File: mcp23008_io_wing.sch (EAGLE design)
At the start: 16 parts

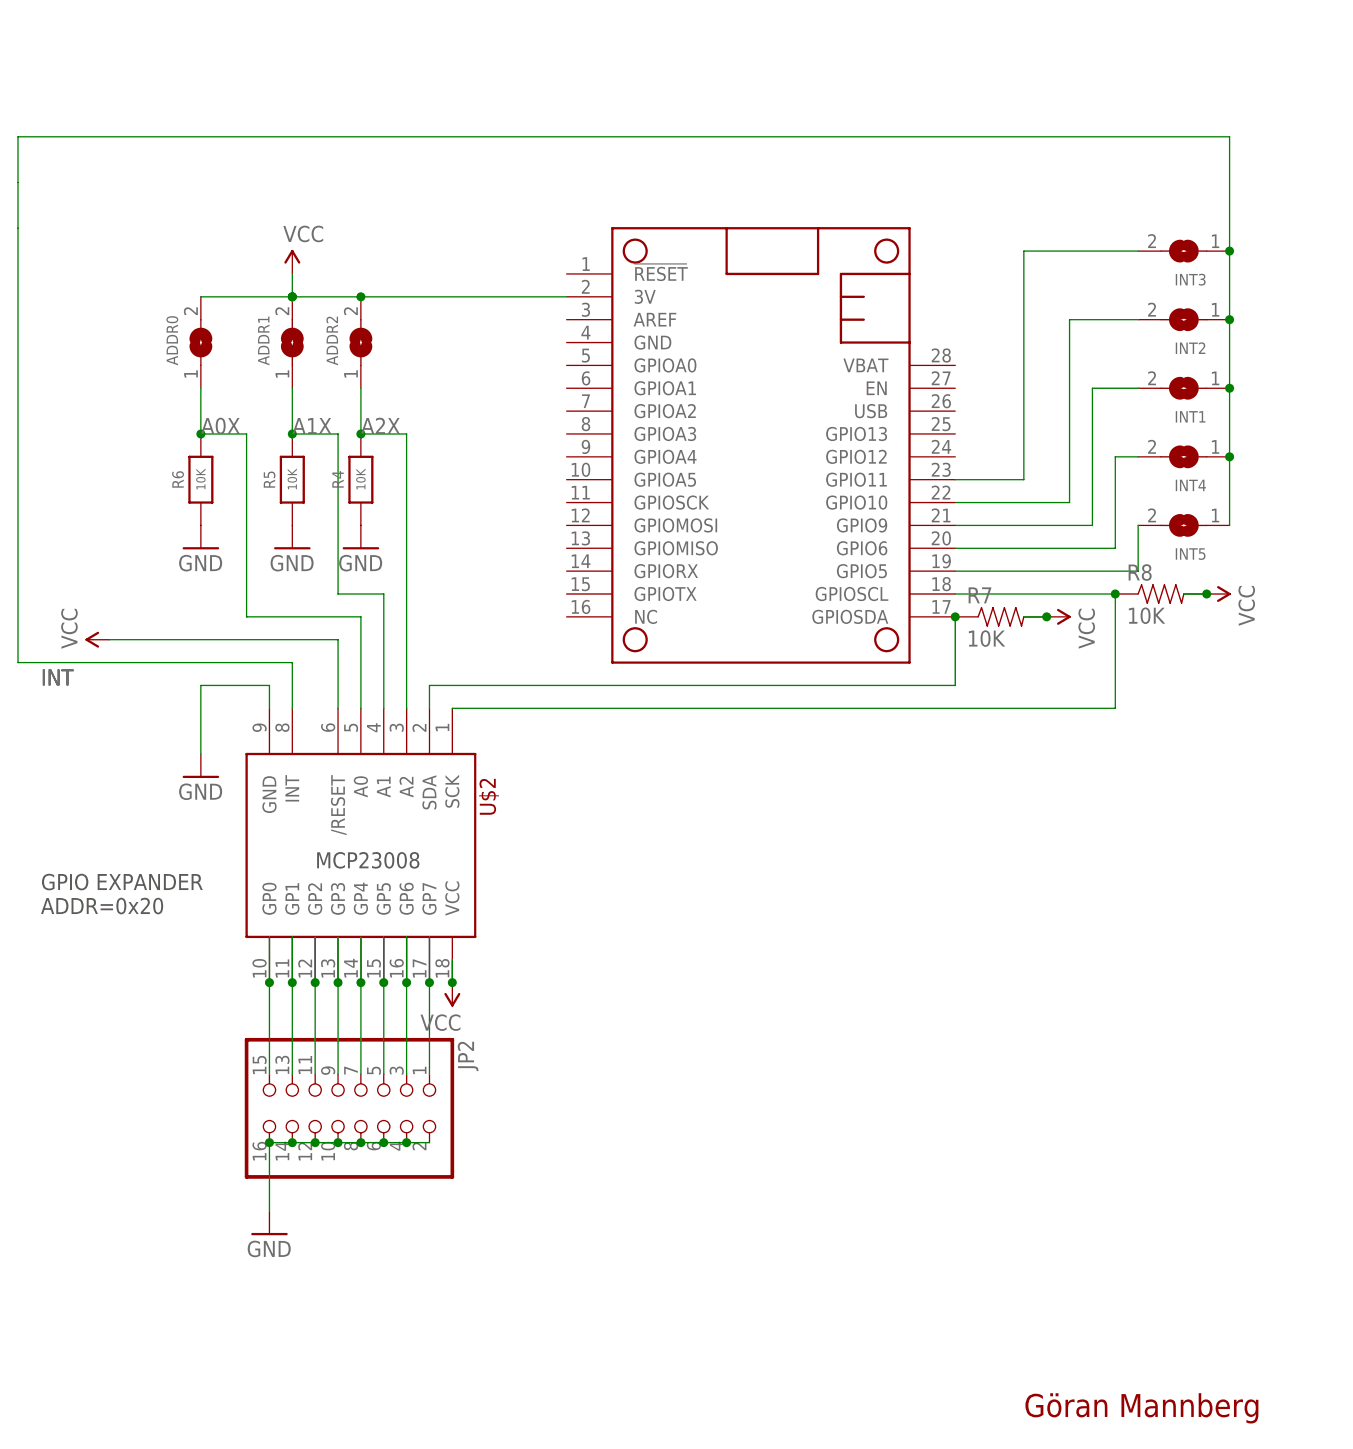
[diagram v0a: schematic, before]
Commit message: updated board and pcb images
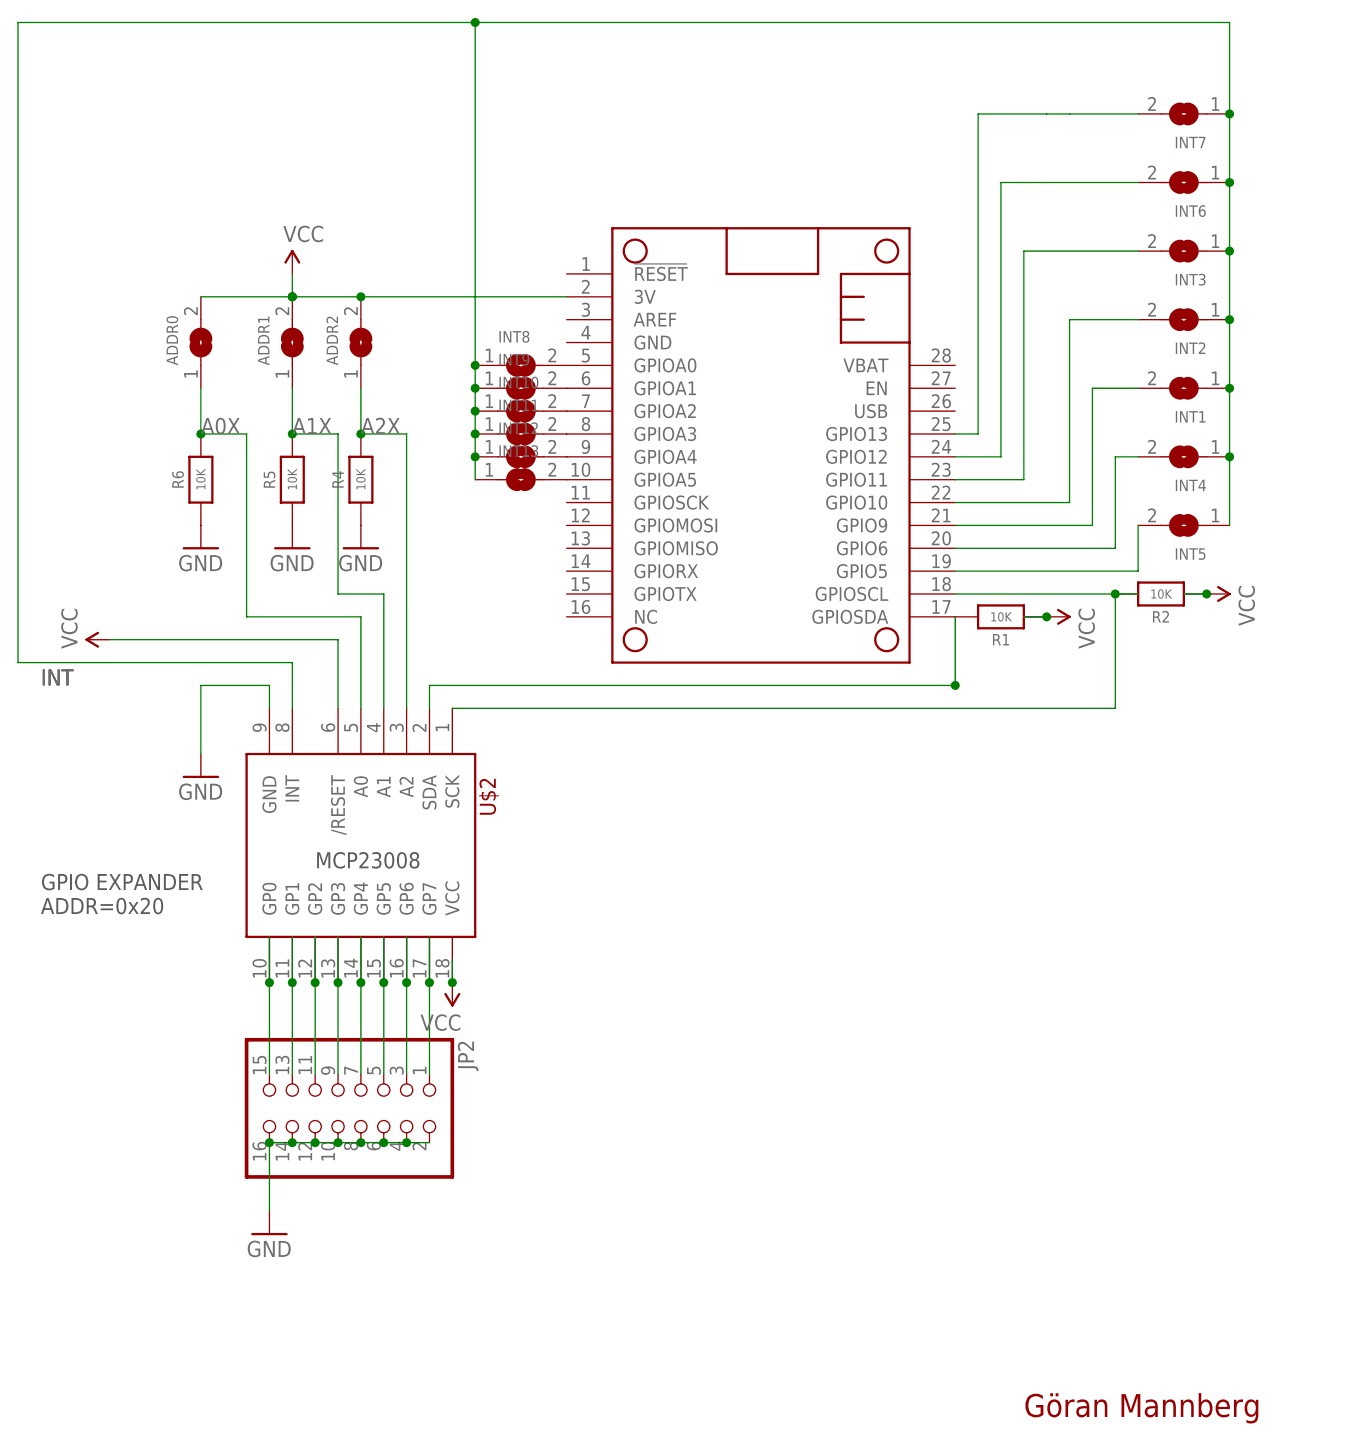
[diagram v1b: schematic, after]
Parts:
- removed R7, R8: 10K, rickk2:RES-10K-06030603
- added INT10, INT11, INT12, INT13, INT6, INT7, INT8, INT9: (no value), microbuilder:SOLDERJUMPER
- added R1, R2: 10K, microbuilder:RESISTOR_0603_NOOUT
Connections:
- new net N$10: INT10.2, MS1.GPIOA2
- new net N$11: INT11.2, MS1.GPIOA3
- new net N$12: INT12.2, MS1.GPIOA4
- new net N$13: INT13.2, MS1.GPIOA5
- new net N$4: INT6.2, MS1.GPIO12
- new net N$5: INT7.2, MS1.GPIO13
- new net N$6: INT8.2, MS1.GPIOA0
- new net N$9: INT9.2, MS1.GPIOA1
- net 3V: now also R1.1, R2.1; no longer R7.2, R8.2
- net INT: now also INT10.1, INT11.1, INT12.1, INT13.1, INT6.1, INT7.1, INT8.1, INT9.1
- net SCL: now also R2.2; no longer R8.1
- net SDA: now also R1.2; no longer R7.1

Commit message: pcb v2
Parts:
- removed R1, R2: 10K, microbuilder:RESISTOR_0603_NOOUT
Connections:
- removed net VCC: U$2./RESET
- net 3V: now also U$2./RESET; no longer R1.1, R2.1
- net SCL: no longer R2.2
- net SDA: no longer R1.2
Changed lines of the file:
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@@
 <part name="SUPPLY1" library="rickk2" deviceset="VCC" device=""/>
 <part name="GND3" library="rickk2" deviceset="GND" device=""/>
-<part name="SUPPLY2" library="rickk2" deviceset="VCC" device=""/>
-<part name="SUPPLY3" library="rickk2" deviceset="VCC" device=""/>
 <part name="SUPPLY4" library="rickk2" deviceset="VCC" device=""/>
-<part name="SUPPLY5" library="rickk2" deviceset="VCC" device=""/>
 <part name="JP2" library="microbuilder" deviceset="HEADER-2X8" device="_SHROUDED"/>
 <part name="GND2" library="rickk2" deviceset="GND" device=""/>
@@
 <part name="INT12" library="microbuilder" deviceset="SOLDERJUMPER" device=""/>
 <part name="INT13" library="microbuilder" deviceset="SOLDERJUMPER" device=""/>
-<part name="R1" library="microbuilder" deviceset="RESISTOR" device="_0603_NOOUT" value="10K"/>
-<part name="R2" library="microbuilder" deviceset="RESISTOR" device="_0603_NOOUT" value="10K"/>
 </parts>
 <sheets>
@@
 <attribute name="VALUE" x="68.58" y="73.66" size="1.778" layer="96"/>
 </instance>
-<instance part="SUPPLY2" gate="G$1" x="182.88" y="96.52" smashed="yes" rot="R270">
-<attribute name="VALUE" x="186.436" y="97.536" size="1.778" layer="96" rot="R270"/>
-</instance>
-<instance part="SUPPLY3" gate="G$1" x="165.1" y="93.98" smashed="yes" rot="R270">
-<attribute name="VALUE" x="168.656" y="94.996" size="1.778" layer="96" rot="R270"/>
-</instance>
 <instance part="SUPPLY4" gate="G$1" x="99.06" y="53.34" smashed="yes" rot="R180">
 <attribute name="VALUE" x="100.076" y="49.784" size="1.778" layer="96" rot="R180"/>
-</instance>
-<instance part="SUPPLY5" gate="G$1" x="60.96" y="91.44" smashed="yes" rot="R90">
-<attribute name="VALUE" x="57.404" y="90.424" size="1.778" layer="96" rot="R90"/>
 </instance>
 <instance part="JP2" gate="G$1" x="88.9" y="38.1" smashed="yes" rot="R270">
@@
 <attribute name="NAME" x="104.14" y="111.76" size="1.27" layer="95"/>
 <attribute name="VALUE" x="104.14" y="105.41" size="1.27" layer="96"/>
-</instance>
-<instance part="R1" gate="G$1" x="160.02" y="93.98" smashed="yes" rot="R180">
-<attribute name="NAME" x="160.02" y="91.44" size="1.27" layer="95" font="vector" rot="R180" align="center"/>
-<attribute name="VALUE" x="160.02" y="93.98" size="1.016" layer="96" font="vector" ratio="15" rot="R180" align="center"/>
-</instance>
-<instance part="R2" gate="G$1" x="177.8" y="96.52" smashed="yes" rot="R180">
-<attribute name="NAME" x="177.8" y="93.98" size="1.27" layer="95" font="vector" rot="R180" align="center"/>
-<attribute name="VALUE" x="177.8" y="96.52" size="1.016" layer="96" font="vector" ratio="15" rot="R180" align="center"/>
 </instance>
 </instances>
@@
 <net name="3V" class="0">
 <segment>
-<wire x1="180.34" y1="96.52" x2="182.88" y2="96.52" width="0.1524" layer="91"/>
-<pinref part="SUPPLY2" gate="G$1" pin="VCC"/>
-<junction x="182.88" y="96.52"/>
-<pinref part="R2" gate="G$1" pin="1"/>
-</segment>
-<segment>
-<wire x1="162.56" y1="93.98" x2="165.1" y2="93.98" width="0.1524" layer="91"/>
-<pinref part="SUPPLY3" gate="G$1" pin="VCC"/>
-<junction x="165.1" y="93.98"/>
-<pinref part="R1" gate="G$1" pin="1"/>
-</segment>
-<segment>
 <wire x1="99.06" y1="55.88" x2="99.06" y2="53.34" width="0.1524" layer="91"/>
 <pinref part="SUPPLY4" gate="G$1" pin="VCC"/>
@@
 <pinref part="ADDR0" gate="1" pin="2"/>
 <wire x1="81.28" y1="129.54" x2="71.12" y2="129.54" width="0.1524" layer="91"/>
+<pinref part="U$2" gate="G$1" pin="/RESET"/>
+<wire x1="86.36" y1="83.82" x2="86.36" y2="91.44" width="0.1524" layer="91"/>
+<wire x1="86.36" y1="91.44" x2="60.96" y2="91.44" width="0.1524" layer="91"/>
+<wire x1="60.96" y1="91.44" x2="60.96" y2="132.08" width="0.1524" layer="91"/>
+<wire x1="60.96" y1="132.08" x2="81.28" y2="132.08" width="0.1524" layer="91"/>
+<junction x="81.28" y="132.08"/>
 </segment>
 </net>
@@
 <pinref part="U$2" gate="G$1" pin="SCK"/>
 <wire x1="99.06" y1="83.82" x2="172.72" y2="83.82" width="0.1524" layer="91"/>
-<junction x="172.72" y="96.52"/>
 <wire x1="172.72" y1="83.82" x2="172.72" y2="96.52" width="0.1524" layer="91"/>
-<pinref part="R2" gate="G$1" pin="2"/>
-<wire x1="175.26" y1="96.52" x2="172.72" y2="96.52" width="0.1524" layer="91"/>
 </segment>
 </net>
@@
 <wire x1="96.52" y1="83.82" x2="96.52" y2="86.36" width="0.1524" layer="91"/>
 <wire x1="154.94" y1="86.36" x2="96.52" y2="86.36" width="0.1524" layer="91"/>
-<pinref part="R1" gate="G$1" pin="2"/>
 <wire x1="154.94" y1="93.98" x2="154.94" y2="86.36" width="0.1524" layer="91"/>
 <junction x="154.94" y="86.36"/>
@@
 </segment>
 </net>
-<net name="VCC" class="0">
-<segment>
-<pinref part="U$2" gate="G$1" pin="/RESET"/>
-<wire x1="86.36" y1="83.82" x2="86.36" y2="91.44" width="0.1524" layer="91"/>
-<pinref part="SUPPLY5" gate="G$1" pin="VCC"/>
-<wire x1="60.96" y1="91.44" x2="86.36" y2="91.44" width="0.1524" layer="91"/>
-</segment>
-</net>
